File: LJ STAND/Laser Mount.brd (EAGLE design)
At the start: 160 x 100 mm, 1 part

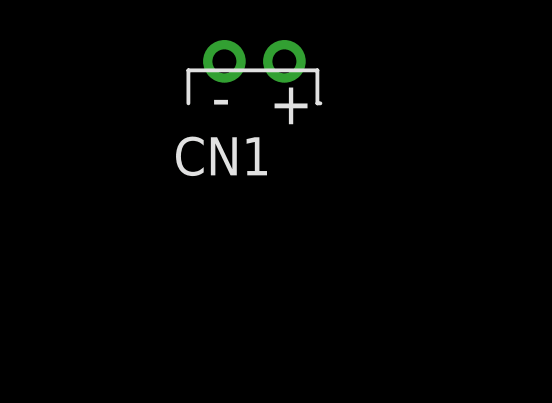
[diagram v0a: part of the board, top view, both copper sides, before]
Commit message: Gyro MPU9250 boards
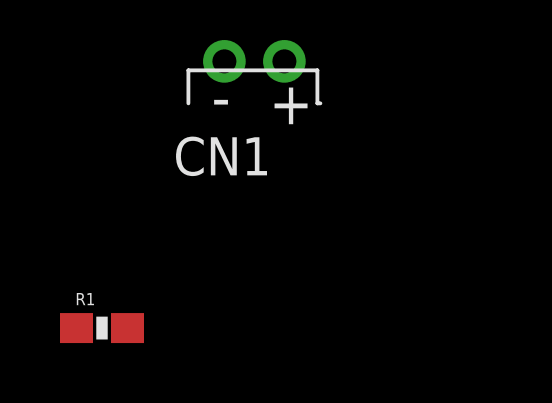
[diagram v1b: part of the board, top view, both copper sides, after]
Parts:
- added R1: (no value), SparkFun-Resistors:0603-RES
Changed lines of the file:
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@@
 <elements>
 <element name="CN1" library="adafruit" package="JST-PH-2-THM-RA" value="" x="-16.51" y="5.08"/>
+<element name="R1" library="SparkFun-Resistors" package="0603-RES" value="" x="-21.59" y="-3.81"/>
 </elements>
 <signals>
